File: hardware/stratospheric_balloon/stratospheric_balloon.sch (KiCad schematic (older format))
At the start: 14 parts, among them M1 CC1101_MODULE, M2 MPU6050_MODULE, M3 BME280_MODULE, M4 STM32_BLUE-PILL_MODULE

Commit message: Add some components for GSM and MCU
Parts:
- added C? (x10): 22p, symbol C_Small
- added J?: SIM_Card, symbol SIM_Card
- added J?: SD_Card, 10067847-001, symbol SD_Card
- added J?: Conn_01x02, symbol Conn_01x02
- added J?: Conn_01x04, symbol Conn_01x04
- added Q?: Q_NPN_BCE, symbol Q_NPN_BCE
- added Q?: Q_NMOS_DGS, symbol Q_NMOS_DGS
- added R? (x17): R, symbol R
- added SW?: SW_Push, symbol SW_Push
- added U?: LM1117-3.3, symbol LM1117-3.3
- added Y? (x2): Crystal, symbol Crystal
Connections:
- net labels added: 32KHZ_A, 32KHZ_B, 8MHZ_A, 8MHZ_B, GSM_PWRKEY, GSM_RX, GSM_SIM_CLK, GSM_SIM_DATA, GSM_SIM_RST, GSM_SIM_VDD, GSM_TX, PWRKEY, SWD_CLK, SWD_IO
- wire segments 87 -> 195
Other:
- note added: "SWD"
- note added: "The power supply range of SIM800C is from 3.4V to 4.4V. Recommended voltage is 4.0V. The transmitting\nburst will cause voltage drop and the power supply must be able to provide sufficient current up to 2A. For the\nVBAT input, a bypass capacitor (low ESR) such as a 100 µF is strongly recommended."
- note removed: "---"
- note removed: "1 +3.3V"
- note removed: "1 INT"
- note removed: "1 SDO"
- note removed: "15 PA5"
- note removed: "16 PA6+18 PB0"
- note removed: "17 PA7\n"
- note removed: "2 ADD"
- note removed: "2 SCB"
- note removed: "2 SI"
- note removed: "25 BME_NSS2"
- note removed: "27 PB14"
- note removed: "28 PB15"
- note removed: "29 PA8"
- note removed: "3 SCK"
- note removed: "3 SDA"
- note removed: "3 XCL"
- note removed: "30 PA9"
- note removed: "31 PA9"
- note removed: "32 PA11"
- note removed: "38 PA11"
- note removed: "4 SCL"
- note removed: "4 SO"
- note removed: "4 XDA"
- note removed: "42 PB6"
- note removed: "43 PB7"
- note removed: "5 GDO2"
- note removed: "5 GND"
- note removed: "5 SDA"
- note removed: "6 GND"
- note removed: "6 SCL"
- note removed: "6 VCC"
- note removed: "7 GDO0"
- note removed: "7 GND"
- note removed: "8 CSN"
- note removed: "8 VCC"
- note removed: "BME_MISO2"
- note removed: "BME_MOSI2"
- note removed: "BME_NSS2"
- note removed: "BME_SCK2"
- note removed: "CC_GDO0"
- note removed: "CC_GDO2"
- note removed: "CC_MISO1"
- note removed: "CC_MOSI1"
- note removed: "CC_NSS1"
- note removed: "CC_SCK1"
- note removed: "M1 CC1101"
- note removed: "M2 MPU6050"
- note removed: "M3 BME280"
- note removed: "M4 BluePill"
- note removed: "MPU_INT"
- note removed: "MPU_SCL1"
- note removed: "MPU_SDA1"
- note removed: "Signal"
- moved on the sheet: BT?, M2, M3, M?

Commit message: Put all components on A4. Do connectians.
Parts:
- removed BT1: 2xAA, symbol 2xAA
- removed LD1: LAZER_DIOD, symbol LAZER_DIOD
- removed M1: CC1101_MODULE, symbol CC1101_MODULE
- removed M4: STM32_BLUE-PILL_MODULE, symbol STM32_BLUE-PILL_MODULE
- added C3, C6, C8, C9: (no value), symbol C_Small
- added J2: UFL, symbol UFL
- added J4: Conn_01x03, symbol Conn_01x03
- added M3: CC1101_MODULE_MIDDLE, symbol CC1101_MODULE_MIDDLE
- R1: renamed from R?; footprint (none) -> Resistors_SMD:R_0603
- gave numbers to parts that had none: 44
- renumbered M2 to M4, M3 to M5
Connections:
- net labels added: +VBAT, BURN_EN, CON_RX, CON_TX, SD_MISO, SD_MOSI, SD_NSS, SD_SCK
- net labels removed: 32KHZ_A, 32KHZ_B, 8MHZ_A, 8MHZ_B, LASER_EN
- wire segments 195 -> 188
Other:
- note added: "CHANGES!!!"
- note added: "MPU_INT: PA9 -> PA8\nCC_GDO0: PA10 -> PA12\nGSM_TX: PA10\nGSM_RX: PA9"
- note removed: "4.5V/2A\n"
- moved on the sheet: BT1, C1, C10, C11, C12, C13, C14, C15, C16, C17, C18, C2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

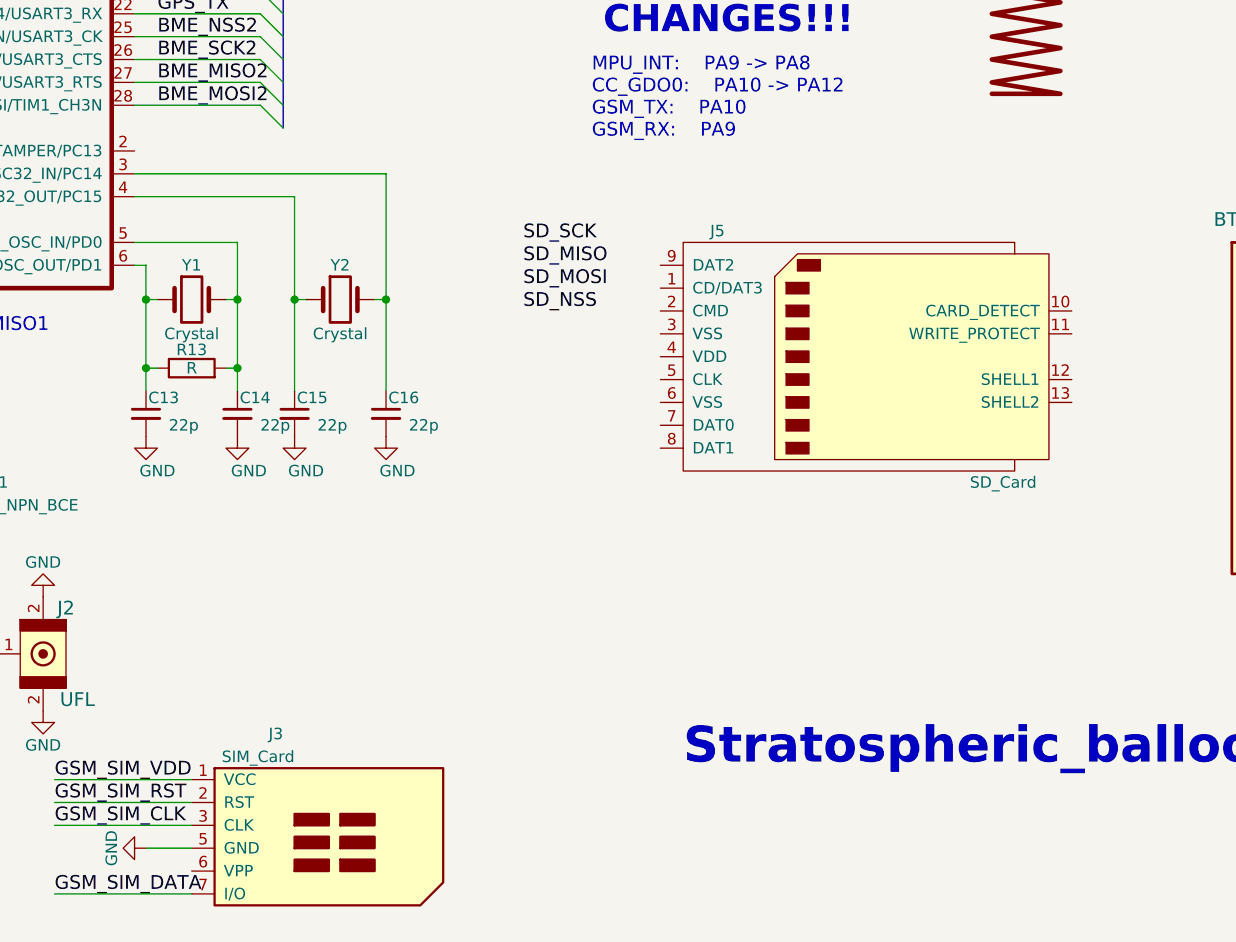
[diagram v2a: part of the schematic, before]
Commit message: Add SIM and microsd slots
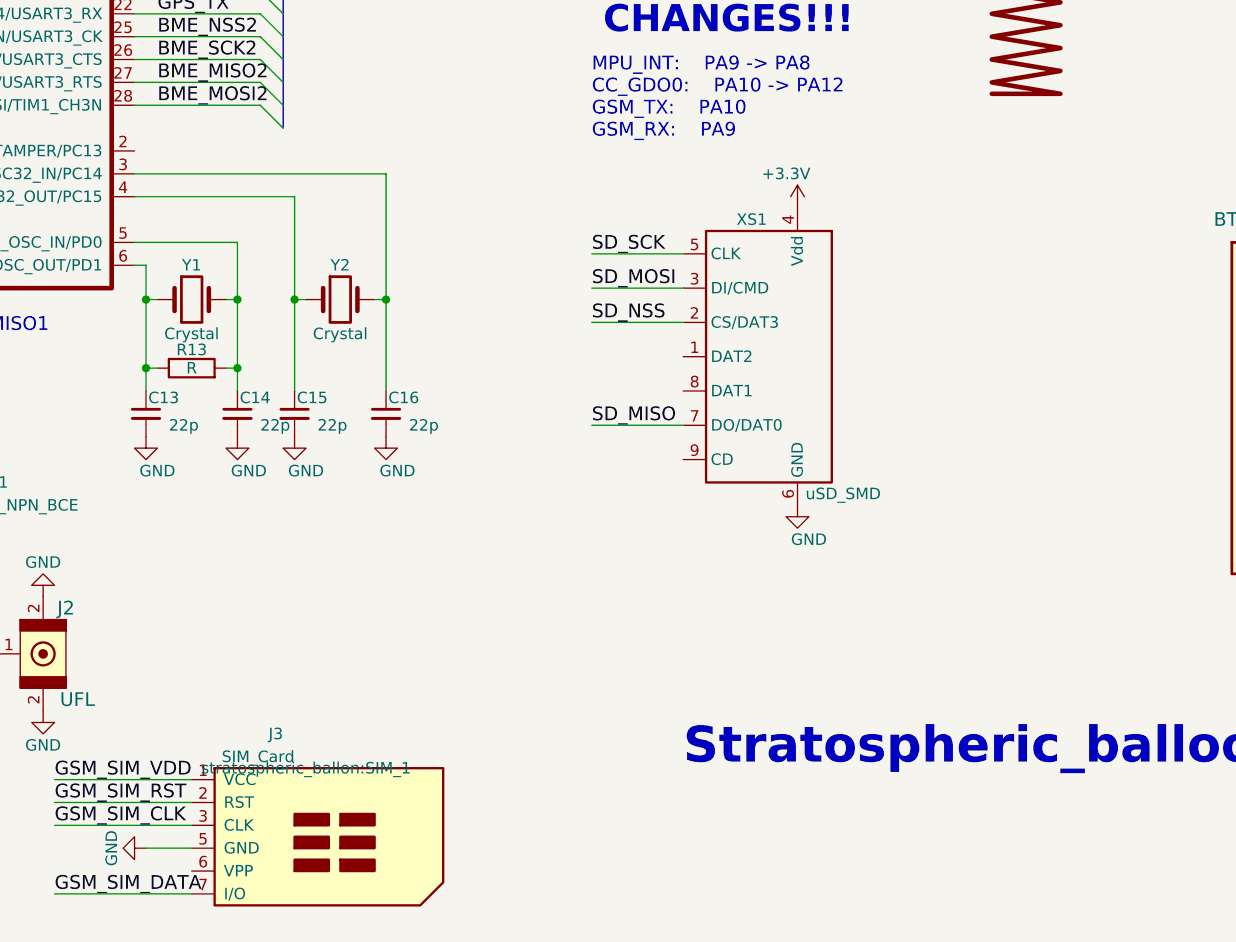
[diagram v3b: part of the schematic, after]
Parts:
- removed J5: SD_Card, 10067847-001, symbol SD_Card
- added XS1: uSD_SMD, stratospheric_ballon:Conn_uSDcard, symbol uSD_SMD
- C1: footprint (none) -> Capacitors_Tantalum_SMD:CP_Tantalum_Case-C_EIA-6032-28_Reflow
- C10, C11, C12, C13, C14, C15, C16, C17, C18, C2, C3, C4, C5, C6, C7, C8, C9: footprint (none) -> Capacitors_SMD:C_0603
- J3: footprint (none) -> stratospheric_ballon:SIM_1
- M1: footprint (none) -> stratospheric_ballon:SIMCom_SIM800C
- Q1: footprint (none) -> TO_SOT_Packages_SMD:SOT-23
- Q2: footprint (none) -> TO_SOT_Packages_SMD:TO-268-2
- R10, R11, R12, R13, R14, R15, R16, R17, R2, R3, R4, R5, R6, R7, R8, R9: footprint (none) -> Resistors_SMD:R_0603
- U2: footprint (none) -> TO_SOT_Packages_SMD:SOT-223
- Y1: footprint (none) -> Crystals:Crystal_HC49-4H_Vertical
- Y2: footprint (none) -> Crystals:Crystal_Round_d2.0mm_Vertical
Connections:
- wire segments 188 -> 192

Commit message: Assign some footprints to sch elements
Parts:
- J1: footprint (none) -> stratospheric_ballon:PinHeader_1x04_P2.54mm_Vertical
- J2: footprint (none) -> stratospheric_ballon:U.FL_Molex_MCRF_73412-0110_Vertical
- J4: footprint (none) -> stratospheric_ballon:PinHeader_1x03_P2.54mm_Vertical
- J6: footprint (none) -> Connectors_Terminal_Blocks:TerminalBlock_bornier-2_P5.08mm
- Q2: footprint TO_SOT_Packages_SMD:TO-268-2 -> TO_SOT_Packages_SMD:SOT-23
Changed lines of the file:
@@
 F 0 "Q2" H 10700 2850 50  0000 L CNN
 F 1 "Q_NMOS_DGS" H 10700 2750 50  0000 L CNN
-F 2 "TO_SOT_Packages_SMD:TO-268-2" H 10700 2900 50  0001 C CNN
+F 2 "TO_SOT_Packages_SMD:SOT-23" H 10700 2900 50  0001 C CNN
 F 3 "" H 10500 2800 50  0001 C CNN
 	1    10500 2800
@@
 F 0 "J6" H 10800 2500 50  0000 C CNN
 F 1 "Conn_01x02" H 10800 2200 50  0000 C CNN
-F 2 "" H 10800 2400 50  0001 C CNN
+F 2 "Connectors_Terminal_Blocks:TerminalBlock_bornier-2_P5.08mm" H 10800 2400 50  0001 C CNN
 F 3 "" H 10800 2400 50  0001 C CNN
 	1    10800 2400
@@
 F 0 "J1" H 950 2100 50  0000 C CNN
 F 1 "Conn_01x04" H 950 1600 50  0000 C CNN
-F 2 "" H 950 1900 50  0001 C CNN
+F 2 "stratospheric_ballon:PinHeader_1x04_P2.54mm_Vertical" H 950 1900 50  0001 C CNN
 F 3 "" H 950 1900 50  0001 C CNN
 	1    950  1900
@@
 F 0 "J4" H 6100 1350 50  0000 C CNN
 F 1 "Conn_01x03" H 6100 950 50  0000 C CNN
-F 2 "" H 6100 1150 50  0001 C CNN
+F 2 "stratospheric_ballon:PinHeader_1x03_P2.54mm_Vertical" H 6100 1150 50  0001 C CNN
 F 3 "" H 6100 1150 50  0001 C CNN
 	1    6100 1150
@@
 F 0 "J2" H 4650 6650 60  0000 C CNN
 F 1 "UFL" H 4700 6250 60  0000 C CNN
-F 2 "" H 4550 6450 60  0001 C CNN
+F 2 "stratospheric_ballon:U.FL_Molex_MCRF_73412-0110_Vertical" H 4550 6450 60  0001 C CNN
 F 3 "" H 4550 6450 60  0001 C CNN
 	1    4550 6450

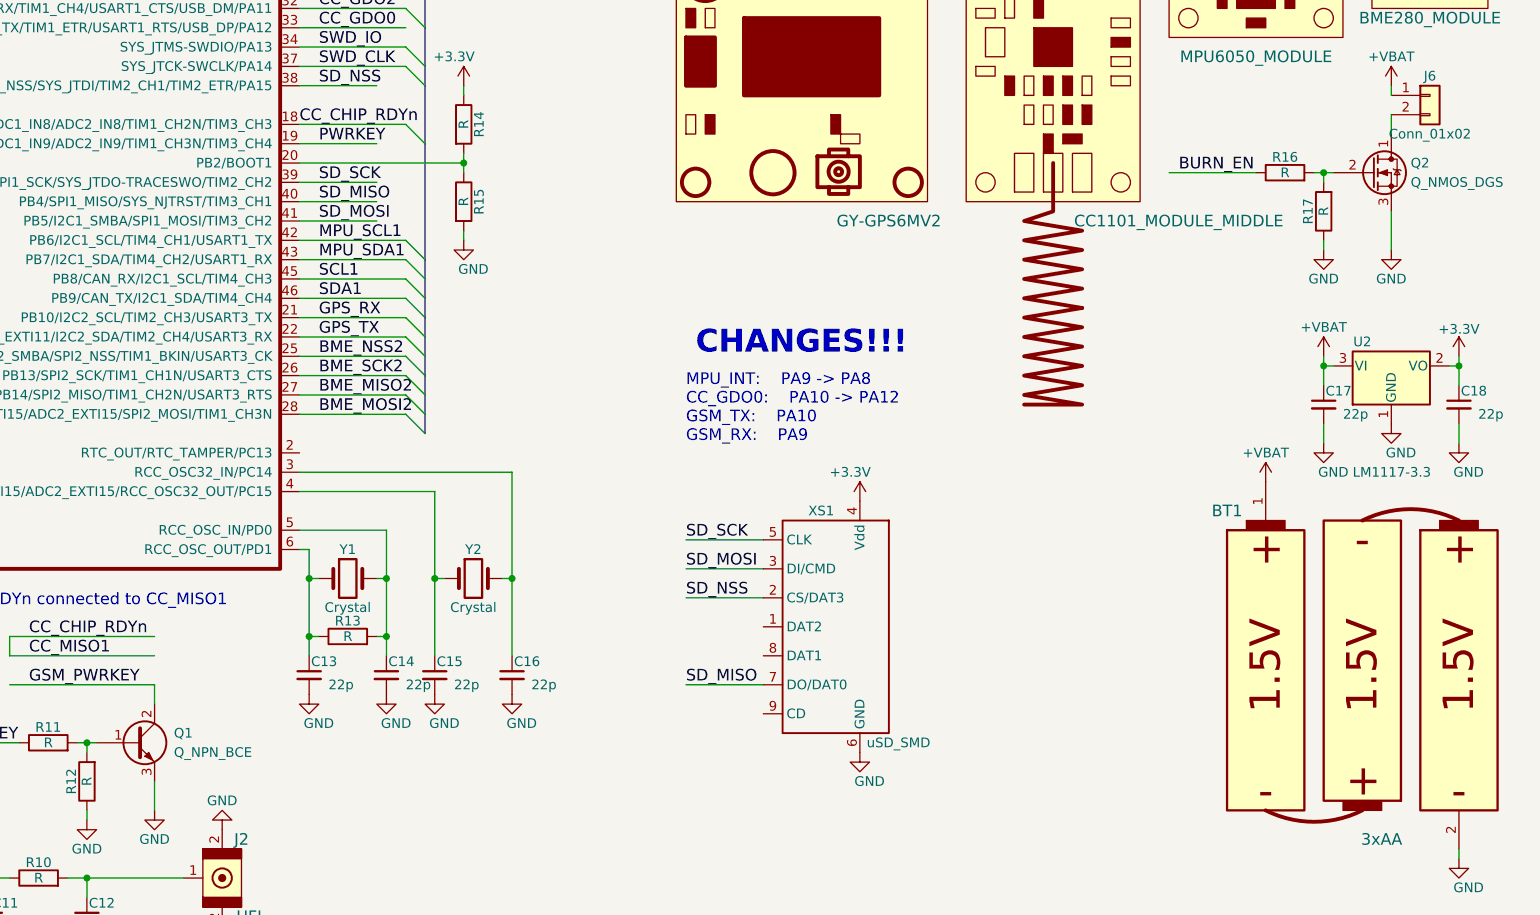
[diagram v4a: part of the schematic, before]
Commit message: Fix mistakes with footprints. Do layout
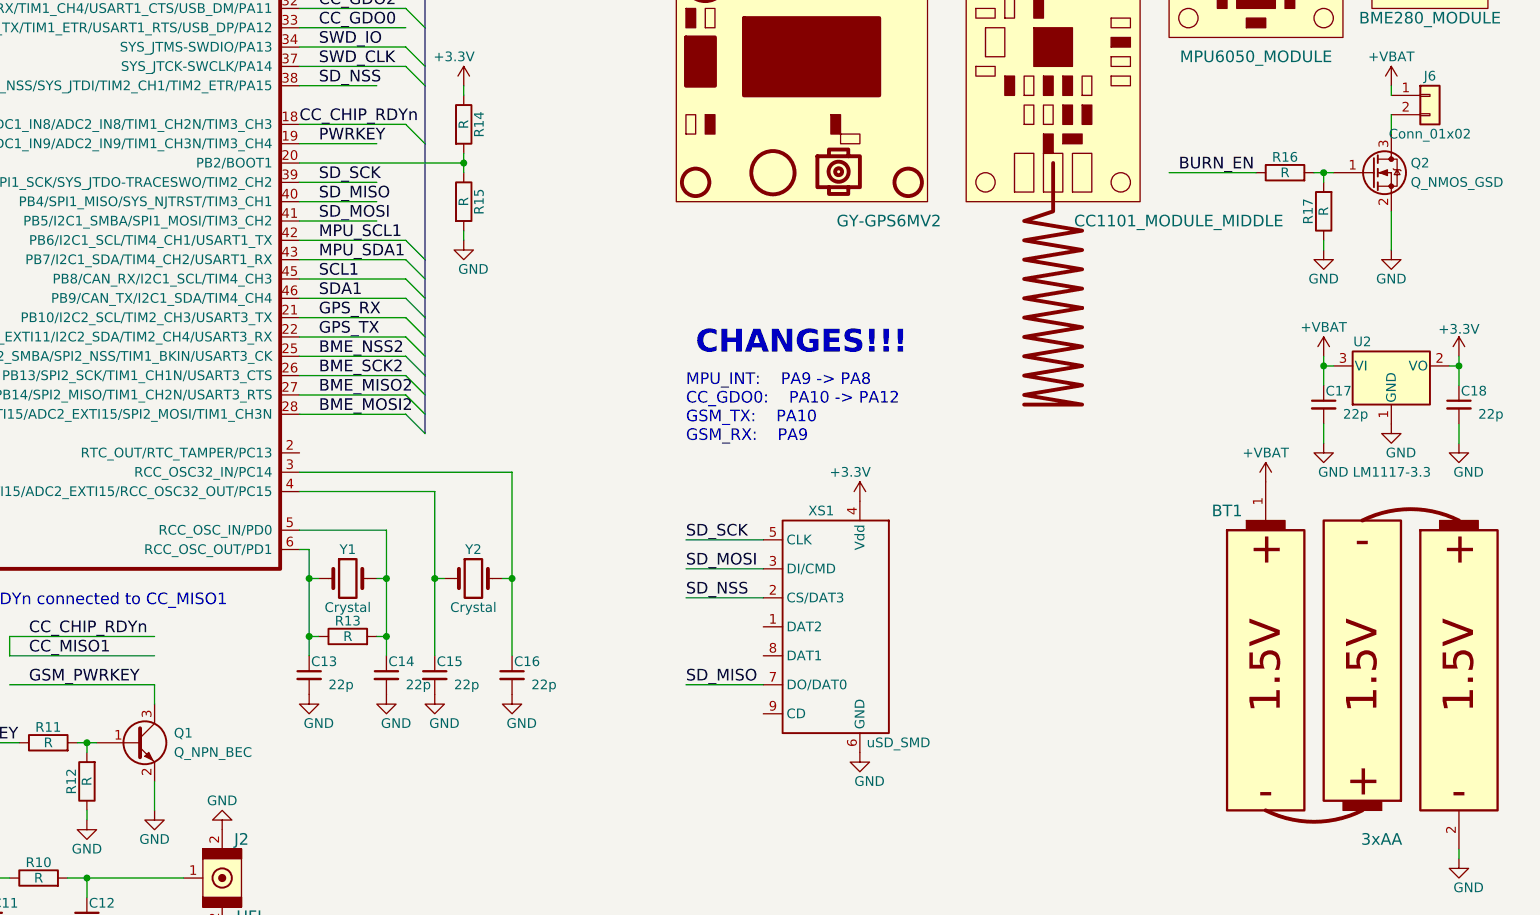
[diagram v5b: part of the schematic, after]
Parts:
- removed Q1: Q_NPN_BCE, TO_SOT_Packages_SMD:SOT-23, symbol Q_NPN_BCE
- removed Q2: Q_NMOS_DGS, TO_SOT_Packages_SMD:SOT-23, symbol Q_NMOS_DGS
- added Q1: Q_NPN_BEC, TO_SOT_Packages_SMD:SOT-23, symbol Q_NPN_BEC
- added Q2: Q_NMOS_GSD, TO_SOT_Packages_SMD:SOT-23, symbol Q_NMOS_GSD
- M2: footprint (none) -> stratospheric_ballon:GY-GPS6MV2_MODULE
- M3: footprint (none) -> stratospheric_ballon:CC1101_MODULE_MIDDLE
- M4: footprint (none) -> stratospheric_ballon:MPU6050_MODULE
- M5: footprint (none) -> stratospheric_ballon:BME280_MODULE
